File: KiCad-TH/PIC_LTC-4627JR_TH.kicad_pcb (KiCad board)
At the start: 2 copper layers, 40.6 x 58.4 mm, 17 parts, among them J1 Conn_01x05_Male, J2 Conn_01x04, Q1 Q_NPN_EBC, Q2 Q_NPN_EBC, Q3 Q_NPN_EBC, Q4 Q_NPN_EBC, Q5 Q_NPN_EBC, U1 PIC16F18344-P

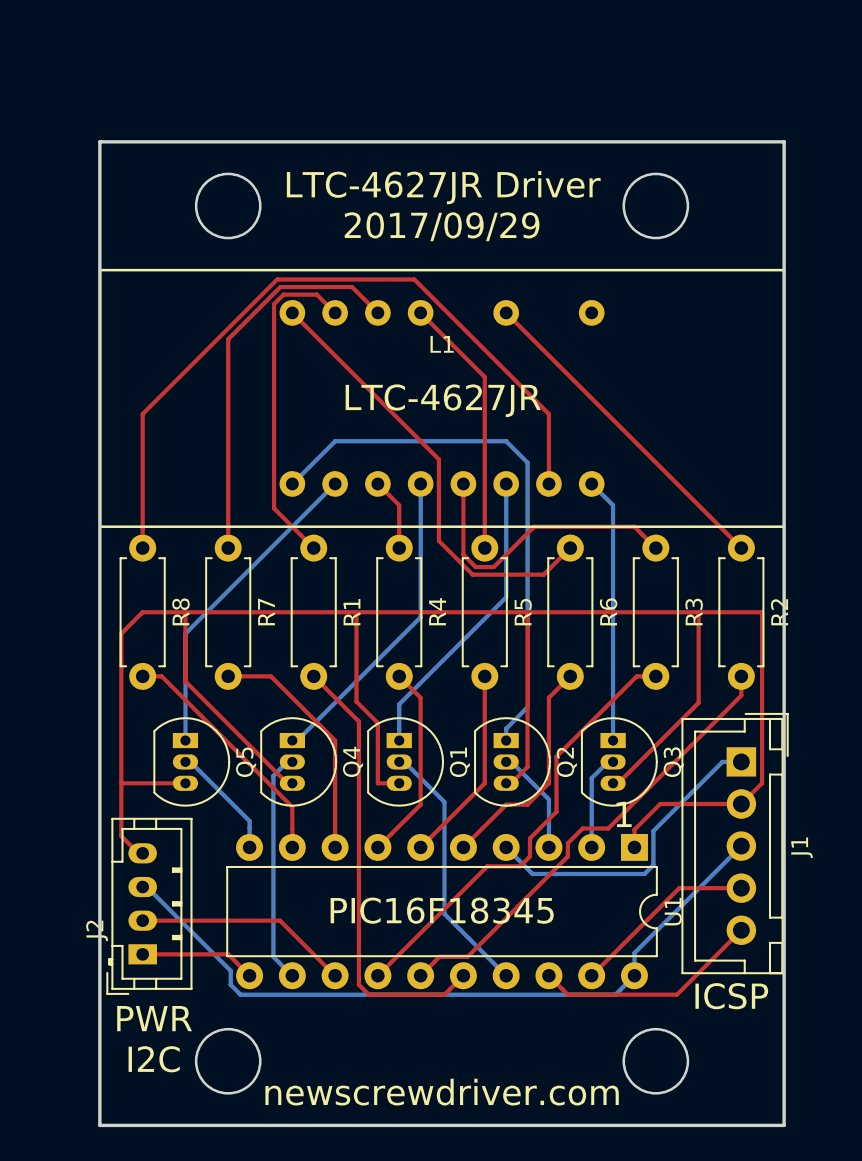
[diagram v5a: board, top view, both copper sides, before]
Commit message: Switch from drawn hole to actual hole component
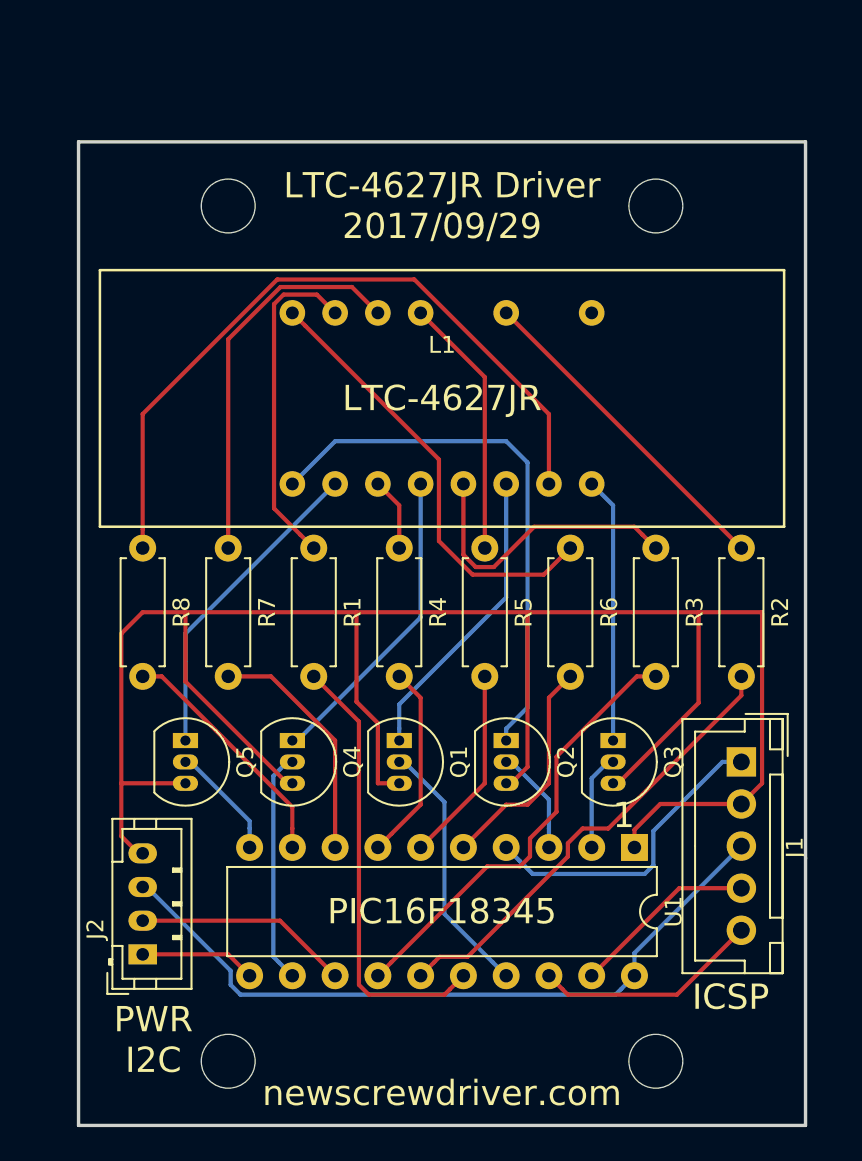
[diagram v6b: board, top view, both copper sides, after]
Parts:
- added H1: MountingHole_3.2mm_M3, Mounting_Holes:MountingHole_3.2mm_M3, F.Cu at (142.2, 82.5)
- added H2: MountingHole_3.2mm_M3, Mounting_Holes:MountingHole_3.2mm_M3, F.Cu at (116.8, 82.5)
- added H3: MountingHole_3.2mm_M3, Mounting_Holes:MountingHole_3.2mm_M3, F.Cu at (142.2, 133.3)
- added H4: MountingHole_3.2mm_M3, Mounting_Holes:MountingHole_3.2mm_M3, F.Cu at (116.8, 133.3)
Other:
- board size 40.6 x 58.4 mm -> 43.2 x 58.4 mm
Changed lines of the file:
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@@
   (general
     (thickness 1.6)
-    (drawings 28)
+    (drawings 24)
     (tracks 176)
     (zones 0)
-    (modules 17)
+    (modules 21)
     (nets 34)
   )
@@
     (0 F.Cu signal)
     (31 B.Cu signal)
-    (32 B.Adhes user)
-    (33 F.Adhes user)
-    (34 B.Paste user)
-    (35 F.Paste user)
+    (32 B.Adhes user hide)
+    (33 F.Adhes user hide)
+    (34 B.Paste user hide)
+    (35 F.Paste user hide)
     (36 B.SilkS user)
     (37 F.SilkS user)
     (38 B.Mask user)
     (39 F.Mask user)
-    (40 Dwgs.User user)
-    (41 Cmts.User user)
-    (42 Eco1.User user)
-    (43 Eco2.User user)
+    (40 Dwgs.User user hide)
+    (41 Cmts.User user hide)
+    (42 Eco1.User user hide)
+    (43 Eco2.User user hide)
     (44 Edge.Cuts user)
-    (45 Margin user)
-    (46 B.CrtYd user)
-    (47 F.CrtYd user)
-    (48 B.Fab user)
+    (45 Margin user hide)
+    (46 B.CrtYd user hide)
+    (47 F.CrtYd user hide)
+    (48 B.Fab user hide)
     (49 F.Fab user)
   )
@@
     (add_net VCC)
   )
+  (module Mounting_Holes:MountingHole_3.2mm_M3 (layer F.Cu)
+    (at 116.84 133.35)
+    (descr "Mounting Hole 3.2mm, no annular, M3")
+    (tags "mounting hole 3.2mm no annular m3")
+    (attr virtual)
+    (fp_text reference H4 (at 0 -4.2) (layer F.SilkS) hide
+      (effects (font (size 1 1) (thickness 0.15)))
+    )
+    (fp_text value MountingHole_3.2mm_M3 (at 0 4.2) (layer F.Fab)
+      (effects (font (size 1 1) (thickness 0.15)))
+    )
+    (fp_text user %R (at 0.3 0) (layer F.Fab)
+      (effects (font (size 1 1) (thickness 0.15)))
+    )
+    (fp_circle (center 0 0) (end 3.2 0) (layer Cmts.User) (width 0.15))
+    (fp_circle (center 0 0) (end 3.45 0) (layer F.CrtYd) (width 0.05))
+    (pad 1 np_thru_hole circle (at 0 0) (size 3.2 3.2) (drill 3.2) (layers *.Cu *.Mask))
+  )
+  (module Mounting_Holes:MountingHole_3.2mm_M3 (layer F.Cu)
+    (at 142.24 133.35)
+    (descr "Mounting Hole 3.2mm, no annular, M3")
+    (tags "mounting hole 3.2mm no annular m3")
+    (attr virtual)
+    (fp_text reference H3 (at 0 -4.2) (layer F.SilkS) hide
+      (effects (font (size 1 1) (thickness 0.15)))
+    )
+    (fp_text value MountingHole_3.2mm_M3 (at 0 4.2) (layer F.Fab)
+      (effects (font (size 1 1) (thickness 0.15)))
+    )
+    (fp_text user %R (at 0.3 0) (layer F.Fab)
+      (effects (font (size 1 1) (thickness 0.15)))
+    )
+    (fp_circle (center 0 0) (end 3.2 0) (layer Cmts.User) (width 0.15))
+    (fp_circle (center 0 0) (end 3.45 0) (layer F.CrtYd) (width 0.05))
+    (pad 1 np_thru_hole circle (at 0 0) (size 3.2 3.2) (drill 3.2) (layers *.Cu *.Mask))
+  )
+  (module Mounting_Holes:MountingHole_3.2mm_M3 (layer F.Cu)
+    (at 116.84 82.55)
+    (descr "Mounting Hole 3.2mm, no annular, M3")
+    (tags "mounting hole 3.2mm no annular m3")
+    (attr virtual)
+    (fp_text reference H2 (at 0 -4.2) (layer F.SilkS) hide
+      (effects (font (size 1 1) (thickness 0.15)))
+    )
+    (fp_text value MountingHole_3.2mm_M3 (at 0 4.2) (layer F.Fab)
+      (effects (font (size 1 1) (thickness 0.15)))
+    )
+    (fp_text user %R (at 0.3 0) (layer F.Fab)
+      (effects (font (size 1 1) (thickness 0.15)))
+    )
+    (fp_circle (center 0 0) (end 3.2 0) (layer Cmts.User) (width 0.15))
+    (fp_circle (center 0 0) (end 3.45 0) (layer F.CrtYd) (width 0.05))
+    (pad 1 np_thru_hole circle (at 0 0) (size 3.2 3.2) (drill 3.2) (layers *.Cu *.Mask))
+  )
+  (module Mounting_Holes:MountingHole_3.2mm_M3 (layer F.Cu)
+    (at 142.24 82.55)
+    (descr "Mounting Hole 3.2mm, no annular, M3")
+    (tags "mounting hole 3.2mm no annular m3")
+    (attr virtual)
+    (fp_text reference H1 (at 0 -4.2) (layer F.SilkS) hide
+      (effects (font (size 1 1) (thickness 0.15)))
+    )
+    (fp_text value MountingHole_3.2mm_M3 (at 0 4.2) (layer F.Fab)
+      (effects (font (size 1 1) (thickness 0.15)))
+    )
+    (fp_text user %R (at 0.3 0) (layer F.Fab)
+      (effects (font (size 1 1) (thickness 0.15)))
+    )
+    (fp_circle (center 0 0) (end 3.2 0) (layer Cmts.User) (width 0.15))
+    (fp_circle (center 0 0) (end 3.45 0) (layer F.CrtYd) (width 0.05))
+    (pad 1 np_thru_hole circle (at 0 0) (size 3.2 3.2) (drill 3.2) (layers *.Cu *.Mask))
+  )
   (module LTC-4627JR:LTC-4627JR (layer F.Cu)
     (at 129.54 93.98)
@@
     (descr "JST XH series connector, B05B-XH-A, top entry type, through hole")
     (tags "connector jst xh tht top vertical 2.50mm")
-    (fp_text reference J1 (at 5 -3.5 270) (layer F.SilkS)
+    (fp_text reference J1 (at 5.08 -3.175 270) (layer F.SilkS)
       (effects (font (size 1 1) (thickness 0.15)))
     )
@@
     (effects (font (size 1.5 1.5) (thickness 0.3)) (justify mirror))
   )
-  (gr_line (start 149.86 78.74) (end 109.22 78.74) (layer Edge.Cuts) (width 0.2))
-  (gr_line (start 149.86 137.16) (end 149.86 78.74) (layer Edge.Cuts) (width 0.2))
-  (gr_line (start 109.22 137.16) (end 149.86 137.16) (layer Edge.Cuts) (width 0.2))
-  (gr_line (start 109.22 78.74) (end 109.22 137.16) (layer Edge.Cuts) (width 0.2))
-  (gr_circle (center 142.24 133.35) (end 144.145 133.35) (layer Edge.Cuts) (width 0.15))
-  (gr_circle (center 116.84 133.35) (end 118.745 133.35) (layer Edge.Cuts) (width 0.15))
-  (gr_circle (center 142.24 82.55) (end 144.145 82.55) (layer Edge.Cuts) (width 0.15))
-  (gr_circle (center 116.84 82.55) (end 118.745 82.55) (layer Edge.Cuts) (width 0.15))
+  (gr_line (start 151.13 78.74) (end 107.95 78.74) (layer Edge.Cuts) (width 0.2))
+  (gr_line (start 151.13 137.16) (end 151.13 78.74) (layer Edge.Cuts) (width 0.2))
+  (gr_line (start 107.95 137.16) (end 151.13 137.16) (layer Edge.Cuts) (width 0.2))
+  (gr_line (start 107.95 78.74) (end 107.95 137.16) (layer Edge.Cuts) (width 0.2))
   (segment (start 147.32 125.57) (end 143.494999 129.395001) (width 0.25) (layer F.Cu) (net 1))
   (segment (start 137.015001 129.395001) (end 136.689999 129.069999) (width 0.25) (layer F.Cu) (net 1))

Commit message: VCC and GND now fill zones instead of traces
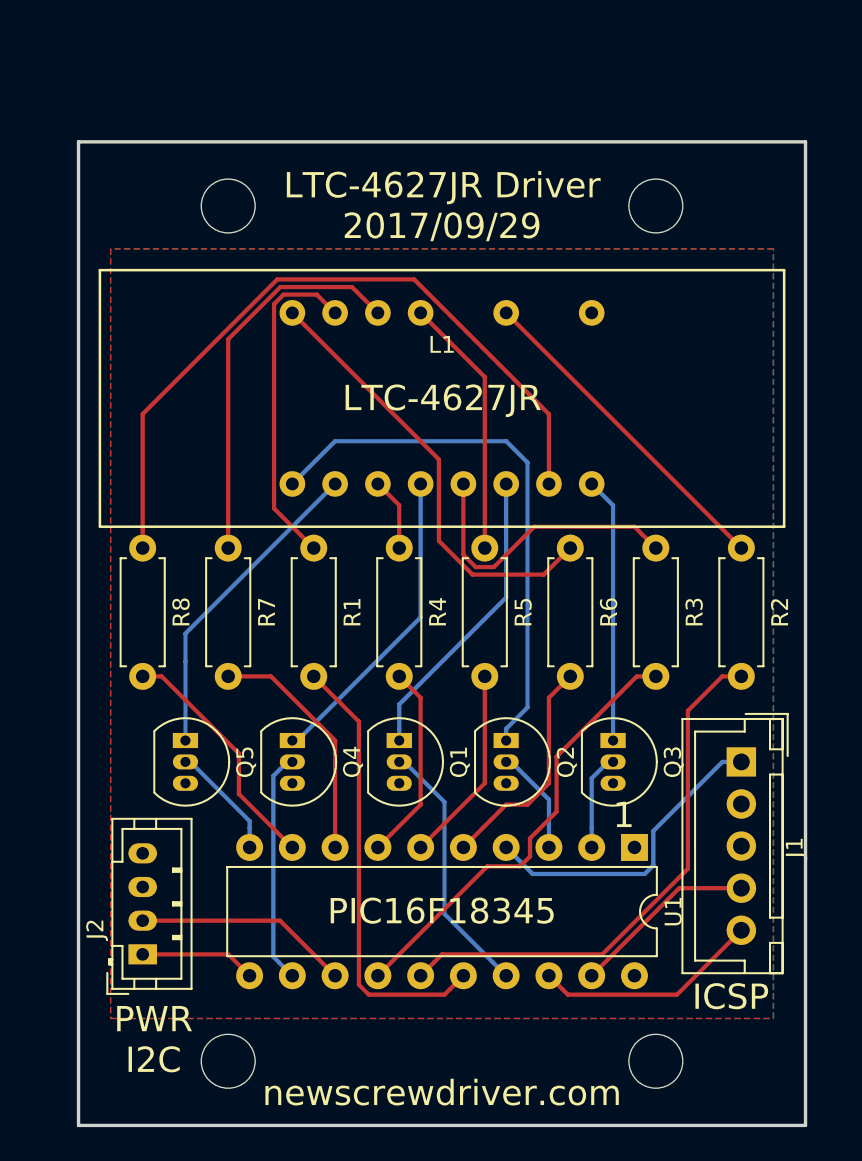
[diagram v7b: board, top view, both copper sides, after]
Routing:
- net VCC: track 123.8 -> 1.15 mm
- net GND: track 43.1 -> 0.25 mm
- net Net-(R2-Pad2): track 27.5 -> 31.9 mm
- added copper zone on B.Cu, net GND
- added copper zone on F.Cu, net VCC
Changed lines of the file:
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@@
     (thickness 1.6)
     (drawings 24)
-    (tracks 176)
+    (tracks 139)
     (zones 0)
     (modules 21)
@@
     (36 B.SilkS user)
     (37 F.SilkS user)
-    (38 B.Mask user)
-    (39 F.Mask user)
+    (38 B.Mask user hide)
+    (39 F.Mask user hide)
     (40 Dwgs.User user hide)
     (41 Cmts.User user hide)
@@
     (47 F.CrtYd user hide)
     (48 B.Fab user hide)
-    (49 F.Fab user)
+    (49 F.Fab user hide)
   )
   (setup
@@
   (segment (start 143.63 123.07) (end 138.43 128.27) (width 0.25) (layer F.Cu) (net 2))
   (segment (start 111.76 123) (end 112.01 123) (width 0.25) (layer B.Cu) (net 3))
-  (segment (start 112.01 123) (end 116.984999 127.974999) (width 0.25) (layer B.Cu) (net 3))
-  (segment (start 116.984999 127.974999) (end 116.984999 128.810001) (width 0.25) (layer B.Cu) (net 3))
-  (segment (start 116.984999 128.810001) (end 117.569999 129.395001) (width 0.25) (layer B.Cu) (net 3))
-  (segment (start 139.844999 129.395001) (end 140.170001 129.069999) (width 0.25) (layer B.Cu) (net 3))
-  (segment (start 117.569999 129.395001) (end 139.844999 129.395001) (width 0.25) (layer B.Cu) (net 3))
-  (segment (start 140.170001 129.069999) (end 140.97 128.27) (width 0.25) (layer B.Cu) (net 3))
-  (segment (start 140.97 128.27) (end 140.97 126.92) (width 0.25) (layer B.Cu) (net 3))
-  (segment (start 140.97 126.92) (end 147.32 120.57) (width 0.25) (layer B.Cu) (net 3))
-  (segment (start 110.49 116.84) (end 110.49 119.98) (width 0.25) (layer F.Cu) (net 4))
-  (segment (start 110.49 119.98) (end 111.51 121) (width 0.25) (layer F.Cu) (net 4))
   (segment (start 111.51 121) (end 111.76 121) (width 0.25) (layer F.Cu) (net 4))
-  (segment (start 134.62 106.68) (end 129.54 106.68) (width 0.25) (layer F.Cu) (net 4))
-  (segment (start 144.78 106.68) (end 134.62 106.68) (width 0.25) (layer F.Cu) (net 4))
-  (segment (start 134.62 106.68) (end 134.62 115.87) (width 0.25) (layer F.Cu) (net 4))
   (segment (start 133.65 116.84) (end 133.35 116.84) (width 0.25) (layer F.Cu) (net 4))
-  (segment (start 134.62 115.87) (end 133.65 116.84) (width 0.25) (layer F.Cu) (net 4))
-  (segment (start 114.3 106.68) (end 111.76 106.68) (width 0.25) (layer F.Cu) (net 4))
-  (segment (start 124.46 106.68) (end 114.3 106.68) (width 0.25) (layer F.Cu) (net 4))
-  (segment (start 114.3 106.68) (end 114.3 110.79) (width 0.25) (layer F.Cu) (net 4))
-  (segment (start 114.3 110.79) (end 120.35 116.84) (width 0.25) (layer F.Cu) (net 4))
   (segment (start 120.35 116.84) (end 120.65 116.84) (width 0.25) (layer F.Cu) (net 4))
-  (segment (start 110.49 107.95) (end 110.49 116.84) (width 0.25) (layer F.Cu) (net 4))
-  (segment (start 110.49 116.84) (end 114.3 116.84) (width 0.25) (layer F.Cu) (net 4))
-  (segment (start 111.76 106.68) (end 110.49 107.95) (width 0.25) (layer F.Cu) (net 4))
   (segment (start 140 116.84) (end 139.7 116.84) (width 0.25) (layer F.Cu) (net 4))
-  (segment (start 148.51 106.68) (end 144.78 106.68) (width 0.25) (layer F.Cu) (net 4))
-  (segment (start 144.78 112.06) (end 140 116.84) (width 0.25) (layer F.Cu) (net 4))
-  (segment (start 144.78 106.68) (end 144.78 112.06) (width 0.25) (layer F.Cu) (net 4))
-  (segment (start 129.54 106.68) (end 124.46 106.68) (width 0.25) (layer F.Cu) (net 4))
-  (segment (start 125.73 116.84) (end 126.54999 116.84) (width 0.25) (layer F.Cu) (net 4))
-  (segment (start 125.73 113.265) (end 125.73 116.84) (width 0.25) (layer F.Cu) (net 4))
-  (segment (start 124.46 106.68) (end 124.46 111.995) (width 0.25) (layer F.Cu) (net 4))
-  (segment (start 124.46 111.995) (end 125.73 113.265) (width 0.25) (layer F.Cu) (net 4))
-  (segment (start 148.55 106.72) (end 148.51 106.68) (width 0.25) (layer F.Cu) (net 4))
-  (segment (start 148.55 116.84) (end 148.55 106.72) (width 0.25) (layer F.Cu) (net 4))
-  (segment (start 147.32 118.07) (end 148.55 116.84) (width 0.25) (layer F.Cu) (net 4))
-  (segment (start 147.32 118.07) (end 142.5 118.07) (width 0.25) (layer F.Cu) (net 4))
-  (segment (start 142.5 118.07) (end 140.97 119.6) (width 0.25) (layer F.Cu) (net 4))
-  (segment (start 140.97 119.6) (end 140.97 120.65) (width 0.25) (layer F.Cu) (net 4))
   (segment (start 147.32 115.57) (end 146.195 115.57) (width 0.25) (layer B.Cu) (net 5))
   (segment (start 146.195 115.57) (end 142.095001 119.669999) (width 0.25) (layer B.Cu) (net 5))
@@
   (segment (start 129.684999 129.395001) (end 130.010001 129.069999) (width 0.25) (layer F.Cu) (net 25))
   (segment (start 130.010001 129.069999) (end 130.81 128.27) (width 0.25) (layer F.Cu) (net 25))
-  (segment (start 147.32 110.49) (end 147.32 111.62137) (width 0.25) (layer F.Cu) (net 26))
-  (segment (start 147.32 111.62137) (end 139.416371 119.524999) (width 0.25) (layer F.Cu) (net 26))
-  (segment (start 137.015001 121.190001) (end 131.060003 127.144999) (width 0.25) (layer F.Cu) (net 26))
-  (segment (start 139.416371 119.524999) (end 137.889999 119.524999) (width 0.25) (layer F.Cu) (net 26))
-  (segment (start 137.889999 119.524999) (end 137.015001 120.399997) (width 0.25) (layer F.Cu) (net 26))
-  (segment (start 137.015001 120.399997) (end 137.015001 121.190001) (width 0.25) (layer F.Cu) (net 26))
-  (segment (start 131.060003 127.144999) (end 129.395001 127.144999) (width 0.25) (layer F.Cu) (net 26))
-  (segment (start 129.395001 127.144999) (end 129.069999 127.470001) (width 0.25) (layer F.Cu) (net 26))
+  (segment (start 147.32 110.49) (end 146.18863 110.49) (width 0.25) (layer F.Cu) (net 26))
+  (segment (start 146.18863 110.49) (end 144.145 112.53363) (width 0.25) (layer F.Cu) (net 26))
+  (segment (start 144.145 121.91859) (end 139.06359 127) (width 0.25) (layer F.Cu) (net 26))
+  (segment (start 139.06359 127) (end 129.54 127) (width 0.25) (layer F.Cu) (net 26))
+  (segment (start 144.145 112.53363) (end 144.145 121.91859) (width 0.25) (layer F.Cu) (net 26))
+  (segment (start 129.54 127) (end 129.069999 127.470001) (width 0.25) (layer F.Cu) (net 26))
   (segment (start 129.069999 127.470001) (end 128.27 128.27) (width 0.25) (layer F.Cu) (net 26))
   (segment (start 142.24 110.49) (end 141.10863 110.49) (width 0.25) (layer F.Cu) (net 27))
@@
   (segment (start 119.38 110.49) (end 123.19 114.3) (width 0.25) (layer F.Cu) (net 31))
   (segment (start 123.19 114.3) (end 123.19 120.65) (width 0.25) (layer F.Cu) (net 31))
+  (segment (start 117.475 115.07363) (end 117.475 117.475) (width 0.25) (layer F.Cu) (net 32))
+  (segment (start 117.475 117.475) (end 120.65 120.65) (width 0.25) (layer F.Cu) (net 32))
   (segment (start 111.76 110.49) (end 112.89137 110.49) (width 0.25) (layer F.Cu) (net 32))
-  (segment (start 112.89137 110.49) (end 120.65 118.24863) (width 0.25) (layer F.Cu) (net 32))
-  (segment (start 120.65 118.24863) (end 120.65 119.51863) (width 0.25) (layer F.Cu) (net 32))
-  (segment (start 120.65 119.51863) (end 120.65 120.65) (width 0.25) (layer F.Cu) (net 32))
+  (segment (start 112.89137 110.49) (end 117.475 115.07363) (width 0.25) (layer F.Cu) (net 32))
   (segment (start 111.76 127) (end 116.84 127) (width 0.25) (layer F.Cu) (net 33))
   (segment (start 116.84 127) (end 118.11 128.27) (width 0.25) (layer F.Cu) (net 33))
+  (zone (net 4) (net_name VCC) (layer F.Cu) (hatch edge 0.508)
+    (connect_pads (clearance 0.508))
+    (min_thickness 0.254)
+    (fill yes (arc_segments 16) (thermal_gap 0.508) (thermal_bridge_width 0.508))
+    (polygon
+      (pts
+        (xy 109.855 130.81) (xy 149.225 130.81) (xy 149.225 85.09) (xy 109.855 85.09)
+      )
+    )
+  )
+  (zone (net 3) (net_name GND) (layer B.Cu) (hatch edge 0.508)
+    (connect_pads (clearance 0.508))
+    (min_thickness 0.254)
+    (fill yes (arc_segments 16) (thermal_gap 0.508) (thermal_bridge_width 0.508))
+    (polygon
+      (pts
+        (xy 109.855 130.81) (xy 149.225 130.81) (xy 149.225 85.09) (xy 109.855 85.09)
+      )
+    )
+  )
 )

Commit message: Erase PCB to start from scratch
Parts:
- removed H1, H2, H3, H4: MountingHole_3.2mm_M3, Mounting_Holes:MountingHole_3.2mm_M3
- removed J1: Conn_01x05_Male, Connectors_JST:JST_XH_B05B-XH-A_05x2.50mm_Straight
- removed J2: Conn_01x04, Connectors_JST:JST_PH_B4B-PH-K_04x2.00mm_Straight
- removed L1: LTC-4627JR, LTC-4627JR:LTC-4627JR
- removed Q1, Q2, Q3, Q4, Q5: Q_NPN_EBC, TO_SOT_Packages_THT:TO-92_Inline_Narrow_Oval
- removed R1, R2, R3, R4, R5, R6, R7, R8: 120, Resistors_THT:R_Axial_DIN0207_L6.3mm_D2.5mm_P7.62mm_Horizontal
- removed U1: PIC16F18344-P, Housings_DIP:DIP-20_W7.62mm
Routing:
- net Net-(L1-Pad7): track 42.9 -> 0.00 mm
- net /DIG_1: track 32.6 -> 0.00 mm
- net Net-(R2-Pad2): track 31.9 -> 0.00 mm
- net Net-(R3-Pad2): track 26.8 -> 0.00 mm
- net Net-(L1-Pad16): track 26.4 -> 0.00 mm
- net Net-(R1-Pad2): track 26.3 -> 0.00 mm
- net Net-(L1-Pad14): track 23.2 -> 0.00 mm
- net Net-(L1-Pad15): track 19.8 -> 0.00 mm
- net Net-(L1-Pad11): track 19.8 -> 0.00 mm
- net /DIG_2: track 18.9 -> 0.00 mm
- net /VPP: track 18.6 -> 0.00 mm
- net /DIG_L: track 18.6 -> 0.00 mm
- net /DIG_3: track 17.9 -> 0.00 mm
- net Net-(L1-Pad5): track 17.5 -> 0.00 mm
- net /DIG_4: track 15.8 -> 0.00 mm
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- removed copper zone on B.Cu, net GND
- removed copper zone on F.Cu, net VCC
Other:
- board outline removed
- rule pad_to_mask_clearance: 0.2 -> 0
- board text removed: "1"
- board text removed: "B"
- board text removed: "C"
- board text removed: "E"
- board text removed: "GND"
- board text removed: "I2CCL"
- board text removed: "I2CDA"
- board text removed: "ICSP"
- board text removed: "ICSPCLK"
- board text removed: "ICSPDAT"
- board text removed: "LTC-4627JR"
- board text removed: "LTC-4627JR Driver 2017/09/29"
- board text removed: "PIC16F18345"
- board text removed: "PWR I2C"
- board text removed: "VCC"
- board text removed: "VPP"
- board text removed: "newscrewdriver.com"
